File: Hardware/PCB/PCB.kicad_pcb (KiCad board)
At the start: 4 copper layers, 74 parts, among them CN1 XT30UPB-M, J1 Connector, USB-TYPE-C-16P, SW1 TS-1187A-B-A-B, U1 RP2350B_C42415655, U10 KF128-2.54-3P, U11 KF128-2.54-3P, U12 KF128-2.54-3P, U2 KF128-2.54-2P, U3 BMP581, U4 ICM-45686, U5 BQ25883RGER, U6 LMR51430YFDDCR, U7 TPS630701RNMR, U8 GD25Q128ESIGR, U9 KF128-2.54-3P, X2 X322512MSB4SI

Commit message: PCB routing started, added BOM.CSV
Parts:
- moved U5 67.4 mm to (35.0, 45.0), turned to -90 degrees
- moved R18 62.8 mm to (29.4, 46.6), turned to -90 degrees
- moved R17 60.2 mm to (31.2, 46.6), turned to -90 degrees
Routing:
- net +5V: track 0.00 -> 18.6 mm, vias 0 -> 6
- net Net-(U1-USB_DP): track 0.00 -> 17.1 mm
- net Net-(D1-Pad6): track 0.00 -> 1.40 mm
- net Net-(D1-Pad4): track 0.00 -> 1.40 mm
- net Net-(D1-Pad3): track 9.35 -> 8.26 mm, vias 2 -> 0
- net Net-(D1-Pad1): track 5.90 -> 5.95 mm, vias 2 -> 0
- added copper zone on In2.Cu, net +5V

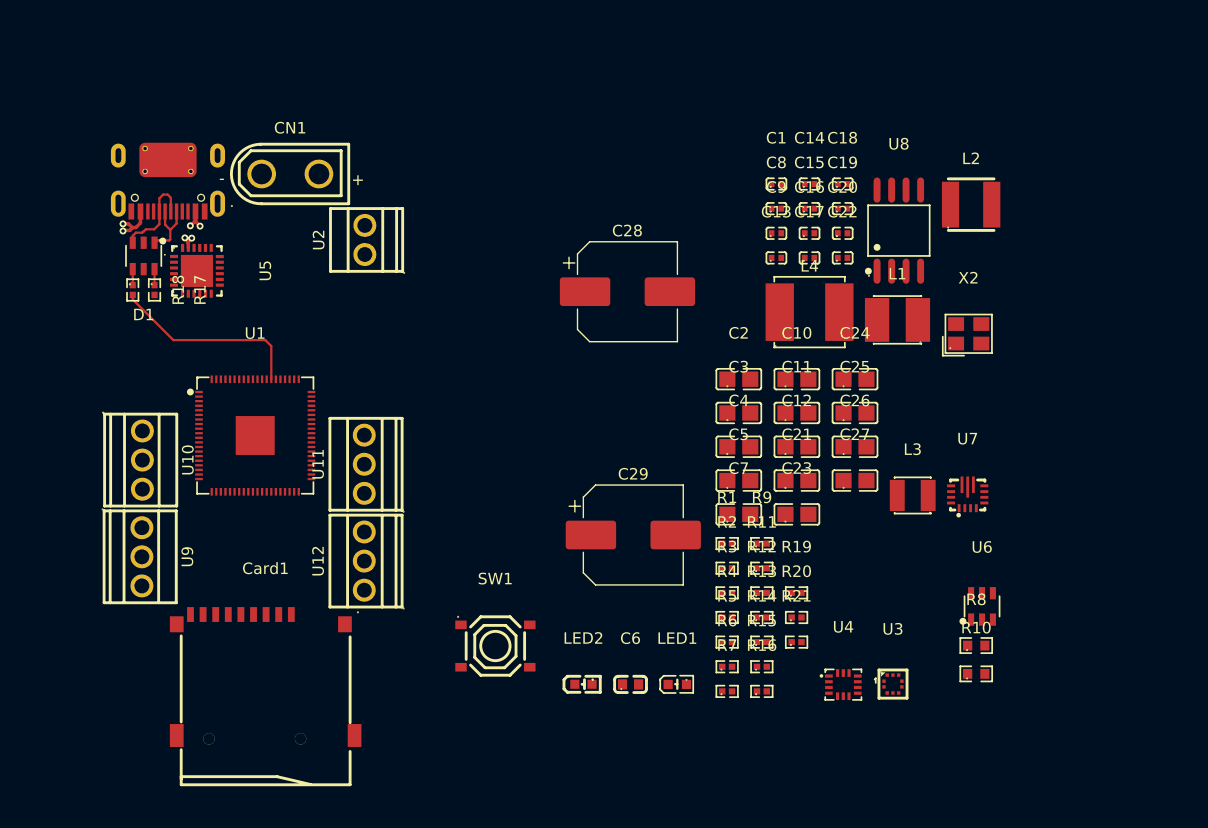
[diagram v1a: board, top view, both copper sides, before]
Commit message: Battery charging added to PCB
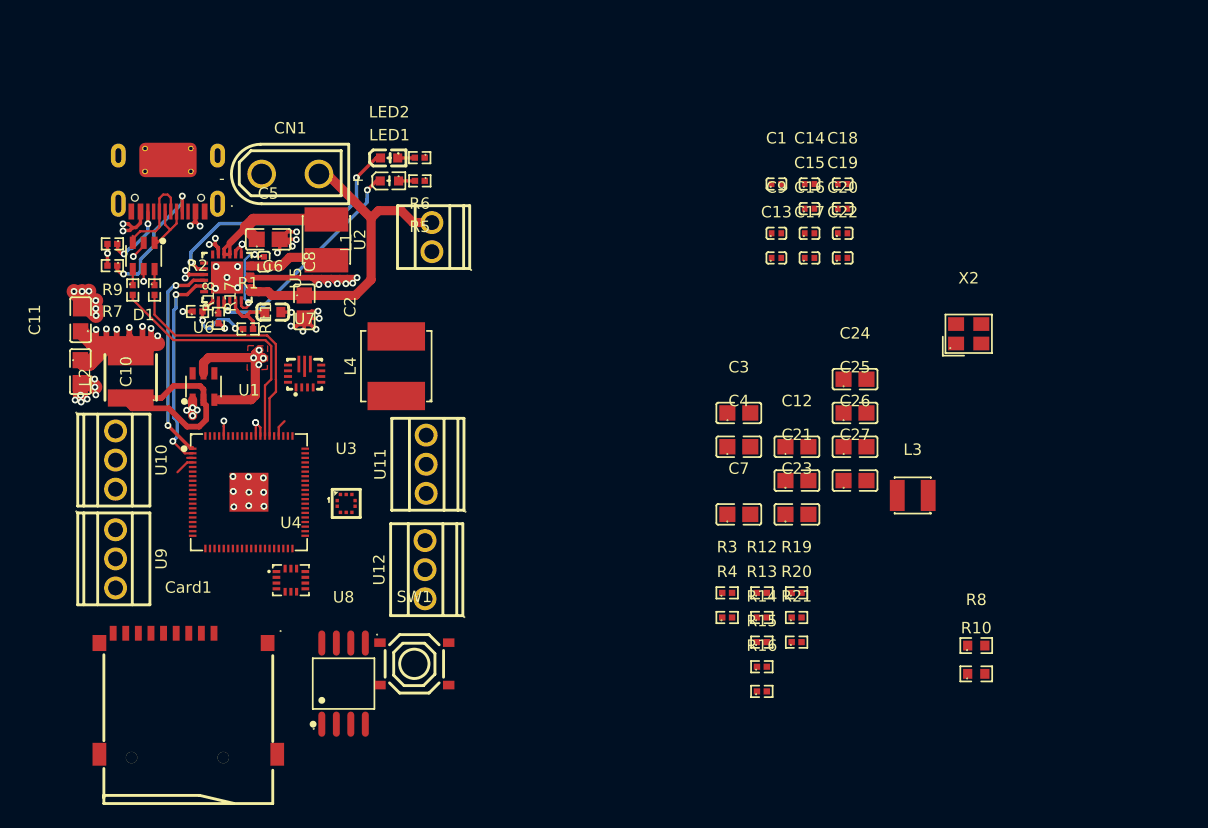
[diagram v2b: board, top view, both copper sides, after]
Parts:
- removed C28, C29: 470 uF, Capacitor_SMD:CP_Elec_8x10.5
- moved L2 74.9 mm to (29.2, 54.2), turned to 90 degrees
- moved U6 70.6 mm to (35.5, 55.0)
- moved R7 65.3 mm to (27.6, 44.5), turned to 180 degrees
- moved C11 63.0 mm to (24.8, 49.2), turned to 90 degrees
- moved C10 62.5 mm to (24.8, 53.8), turned to -90 degrees
- moved U8 62.5 mm to (47.8, 81.0)
- moved R9 62.4 mm to (27.6, 42.6), turned to 180 degrees
- moved U7 58.8 mm to (44.4, 54.1)
- moved R11 52.2 mm to (36.8, 49.1), turned to -90 degrees
- moved R6 51.9 mm to (54.4, 35.1), turned to 180 degrees
- moved R2 51.4 mm to (35.0, 48.5)
- moved LED1 50.6 mm to (51.8, 37.1)
- moved L1 50.3 mm to (46.2, 42.2), turned to -90 degrees
- moved U3 50.3 mm to (48.0, 65.2)
- moved U4 49.1 mm to (43.1, 72.0)
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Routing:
- net +3V3: track 0.00 -> 39.4 mm, vias 0 -> 10
- net +7.5V: track 0.00 -> 38.3 mm, vias 0 -> 10
- net GND: track 0.00 -> 36.3 mm, vias 0 -> 49
- net Net-(CN1-+): track 0.00 -> 30.3 mm
- net Net-(LED2-K): track 0.00 -> 23.6 mm, vias 0 -> 2
- net Net-(U1-USB_DM): track 0.00 -> 21.6 mm
- net Net-(LED1-K): track 0.00 -> 19.6 mm, vias 0 -> 2
- net Net-(U6-SW): track 0.00 -> 19.0 mm
- net Net-(U1-GPIO4): track 0.00 -> 18.2 mm, vias 0 -> 2
- net Net-(U1-GPIO5): track 0.00 -> 18.1 mm, vias 0 -> 2
- net Net-(C5-Pad1): track 0.00 -> 13.2 mm
- net Net-(J1-CC1): track 0.00 -> 12.1 mm, vias 0 -> 2
- net Net-(U5-BTST): track 0.00 -> 7.35 mm, vias 0 -> 2
- net Net-(C8-Pad2): track 0.00 -> 7.04 mm
- net Net-(U5-TS): track 0.00 -> 6.87 mm, vias 0 -> 2
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- added copper zone on In2.Cu, net (none)
- added copper zone on In2.Cu, net +3V3
- added copper zone on F.Cu, net +7.5V
- added copper zone on In1.Cu, net GND

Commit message: Restarting PCB, finished Flash memory application
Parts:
- added C28: CL05B104KO5NNNC, easyeda2kicad:C0402, F.Cu at (105.8, 59.1)
- added C29: CL05B104KO5NNNC, easyeda2kicad:C0402, F.Cu at (105.8, 61.3)
- added C30: CL05B104KO5NNNC, easyeda2kicad:C0402, F.Cu at (108.7, 48.4)
- added C32: CL05B104KO5NNNC, easyeda2kicad:C0402, F.Cu at (108.7, 50.5)
- added C33: CL05B104KO5NNNC, easyeda2kicad:C0402, F.Cu at (108.7, 52.7)
- added C34: CL05B104KO5NNNC, easyeda2kicad:C0402, F.Cu at (108.7, 54.9)
- added C35: CL05B104KO5NNNC, easyeda2kicad:C0402, F.Cu at (108.7, 57.0)
- added C36: CL05B104KO5NNNC, easyeda2kicad:C0402, F.Cu at (108.7, 59.1)
- added C37: CL05B104KO5NNNC, easyeda2kicad:C0402, F.Cu at (108.7, 61.3)
- added C38: CL05B104KO5NNNC, easyeda2kicad:C0402, F.Cu at (111.6, 48.4)
- added C39: CL05B104KO5NNNC, easyeda2kicad:C0402, F.Cu at (111.6, 50.5)
- added C40: CL05B104KO5NNNC, easyeda2kicad:C0402, F.Cu at (111.6, 52.7)
- moved C10 86.6 mm to (109.1, 34.0), turned to 0 degrees
- moved C11 85.2 mm to (109.1, 37.0), turned to 0 degrees
- moved C6 78.6 mm to (119.7, 57.7)
- moved R9 72.4 mm to (96.7, 64.2), turned to 0 degrees
- moved U7 71.1 mm to (115.3, 58.6)
- moved SW1 64.0 mm to (117.7, 73.2)
- moved U4 63.2 mm to (106.2, 67.8)
- moved C5 62.8 mm to (104.0, 42.9)
- moved C8 62.5 mm to (102.9, 50.5), turned to 0 degrees
- moved R11 62.3 mm to (96.7, 66.4), turned to 0 degrees
- moved C2 61.3 mm to (104.0, 34.0), turned to 0 degrees
- moved U3 61.3 mm to (108.4, 75.7)
- moved R2 61.3 mm to (93.6, 66.4)
- moved L2 60.2 mm to (88.9, 61.5), turned to 0 degrees
- moved R1 56.0 mm to (93.6, 64.2)
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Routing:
- net +3V3: track 39.4 -> 1.66 mm, vias 10 -> 1
- net +7.5V: track 38.3 -> 3.46 mm, vias 10 -> 4
- net Net-(LED2-K): track 23.6 -> 0.00 mm, vias 2 -> 0
- net GND: track 36.3 -> 13.9 mm, vias 49 -> 26
- net Net-(LED1-K): track 19.6 -> 0.00 mm, vias 2 -> 0
- net Net-(U6-SW): track 19.0 -> 0.00 mm
- net Net-(U1-GPIO4): track 18.2 -> 0.00 mm, vias 2 -> 0
- net Net-(U1-GPIO5): track 18.1 -> 0.00 mm, vias 2 -> 0
- net Net-(U1-USB_DP): track 22.2 -> 36.7 mm
- net Net-(C5-Pad1): track 13.2 -> 0.00 mm
- net Net-(U1-QSPI_SD3): track 0.00 -> 12.6 mm
- net Net-(U1-USB_DM): track 21.6 -> 34.1 mm
- net Net-(U1-QSPI_SS): track 0.00 -> 12.4 mm
- net +5V: track 19.7 -> 7.82 mm, vias 7 -> 3
- net Net-(U1-QSPI_SCLK): track 0.00 -> 11.2 mm
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- added copper zone on B.Cu, net GND
- added copper zone on F.Cu, net GND
- removed copper zone on In2.Cu, net (none)
- removed copper zone on In2.Cu, net +3V3
- removed copper zone on F.Cu, net +7.5V
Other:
- board outline added: 36.5 x 58 mm

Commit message: Got some advice, restarting entire project, applied integrated inductors to schematic, and restarted it
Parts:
- removed C1: CL05A105KA5NQNC, easyeda2kicad:C0402
- removed C10, C11, C12, C2, C21, C23, C24, C25, C26, C27, C5, C7: CL21A106KAYNNNE, easyeda2kicad:C0805
- removed C13, C14: CC0402JRNPO9BN270, easyeda2kicad:C0402
- removed C15, C16, C17, C18, C19, C20, C22, C28, C29, C30, C32, C33, C34, C35, C36, C37, C38, C39, C40, C9: CL05B104KO5NNNC, easyeda2kicad:C0402
- removed C3, C4: CL21A226MAQNNNE, easyeda2kicad:C0805
- removed C6: CL10A475KO8NNNC, easyeda2kicad:C0603
- removed C8: 0402B473K500NT, easyeda2kicad:C0402
- removed CN1: XT30UPB-M, easyeda2kicad:CONN-TH_XT30UPB-M
- removed Card1: TF-01A, easyeda2kicad:TF-SMD_TF-01A
- removed D1: USBLC6-2SC6, easyeda2kicad:SOT-23-6_L2.9-W1.6-P0.95-LS2.8-BL
- removed J1: Connector, USB-TYPE-C-16P, PCM_JLCPCB:TYPE-C-SMD_HX-TYPE-C-16PIN
- removed L1: SWPA4030S1R0NT, easyeda2kicad:IND-SMD_L4.0-W4.0_SWPA4018S
- removed L2: SMNR4020-2.2UH, easyeda2kicad:IND-SMD_L4.0-W4.0_LQH44PN2R2MP0L
- removed L3: SWPA3015S4R7MT, easyeda2kicad:IND-SMD_L3.0-W3.0_FNR30XXS
- removed L4: SWPA6045S1R5NT, easyeda2kicad:IND-SMD_L6.0-W6.0_SWPA6045S
- removed LED1: 0603White light_C2290, easyeda2kicad:LED0603-R-RD_WHITE
- removed LED2: KT-0603R, easyeda2kicad:LED-SMD_L1.6-W0.8-R-RD
- removed R1, R12, R13, R14, R15, R16, R2, R3, R4: 0402WGF1002TCE, easyeda2kicad:R0402
- removed R10: 0603WAF2202T5E, easyeda2kicad:R0603
- removed R11: 0402WGF2000TCE, easyeda2kicad:R0402
- removed R17, R18: 0402WGF270JTCE, easyeda2kicad:R0402
- removed R19, R5, R6: 0402WGF1001TCE, easyeda2kicad:R0402
- removed R20, R21: 0402WGF4701TCE, easyeda2kicad:R0402
- removed R7, R9: 0402WGF5101TCE, easyeda2kicad:R0402
- removed R8: 0603WAF1003T5E, easyeda2kicad:R0603
- removed SW1: TS-1187A-B-A-B, easyeda2kicad:SW-SMD_4P-L5.1-W5.1-P3.70-LS6.5-TL_H1.5
- removed U1: RP2350B_C42415655, easyeda2kicad:QFN-80_L10.0-W10.0-P0.40-TL-EP3.4
- removed U10, U11, U12, U9: KF128-2.54-3P, easyeda2kicad:CONN-TH_3P-P2.54_KF128-2.54-3P
- removed U2: KF128-2.54-2P, easyeda2kicad:CONN-TH_P2.54_KF128-2.54-2P
- removed U3: BMP581, easyeda2kicad:LGA-10_L2.0-W2.0-P0.50-TL_BMP581
- removed U4: ICM-45686, easyeda2kicad:LGA-14_L3.0-W2.5-P0.50-TL
- removed U5: BQ25883RGER, easyeda2kicad:VFQFPN-24_L4.0-W4.0-P0.50-BL-EP2.8
- removed U6: LMR51430YFDDCR, easyeda2kicad:SOT-23-6_L2.9-W1.6-P0.95-LS2.9-BL
- removed U7: TPS630701RNMR, easyeda2kicad:VQFN-HR-15_L3.0-W2.5-P0.50-BL_TPS63070RNMR
- removed U8: GD25Q128ESIGR, easyeda2kicad:SOP-8_L5.3-W5.3-P1.27-LS8.0-BL
- removed X2: X322512MSB4SI, easyeda2kicad:CRYSTAL-SMD_4P-L3.2-W2.5-BL
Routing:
- net Net-(U1-USB_DP): track 36.7 -> 0.00 mm
- net Net-(U1-USB_DM): track 34.1 -> 0.00 mm
- net Net-(CN1-+): track 19.3 -> 0.00 mm
- net GND: track 13.9 -> 0.00 mm, vias 26 -> 0
- net Net-(U1-QSPI_SD3): track 12.6 -> 0.00 mm
- net Net-(U1-QSPI_SS): track 12.4 -> 0.00 mm
- net Net-(U1-QSPI_SCLK): track 11.2 -> 0.00 mm
- net Net-(U1-QSPI_SD1): track 10.8 -> 0.00 mm
- net +5V: track 7.82 -> 0.00 mm, vias 3 -> 0
- net Net-(U1-QSPI_SD2): track 7.47 -> 0.00 mm
- net Net-(U1-QSPI_SD0): track 7.44 -> 0.00 mm
- net Net-(U1-VREG_LX): track 6.21 -> 0.00 mm
- net Net-(D1-Pad3): track 5.44 -> 0.00 mm
- net Net-(D1-Pad1): track 4.18 -> 0.00 mm
- net +7.5V: track 3.46 -> 0.00 mm, vias 4 -> 0
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- removed copper zone on In2.Cu, net +5V
- removed copper zone on B.Cu, net GND
- removed copper zone on F.Cu, net GND
- removed copper zone on In1.Cu, net GND
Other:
- board outline removed
